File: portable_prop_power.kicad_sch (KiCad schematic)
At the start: 10 parts

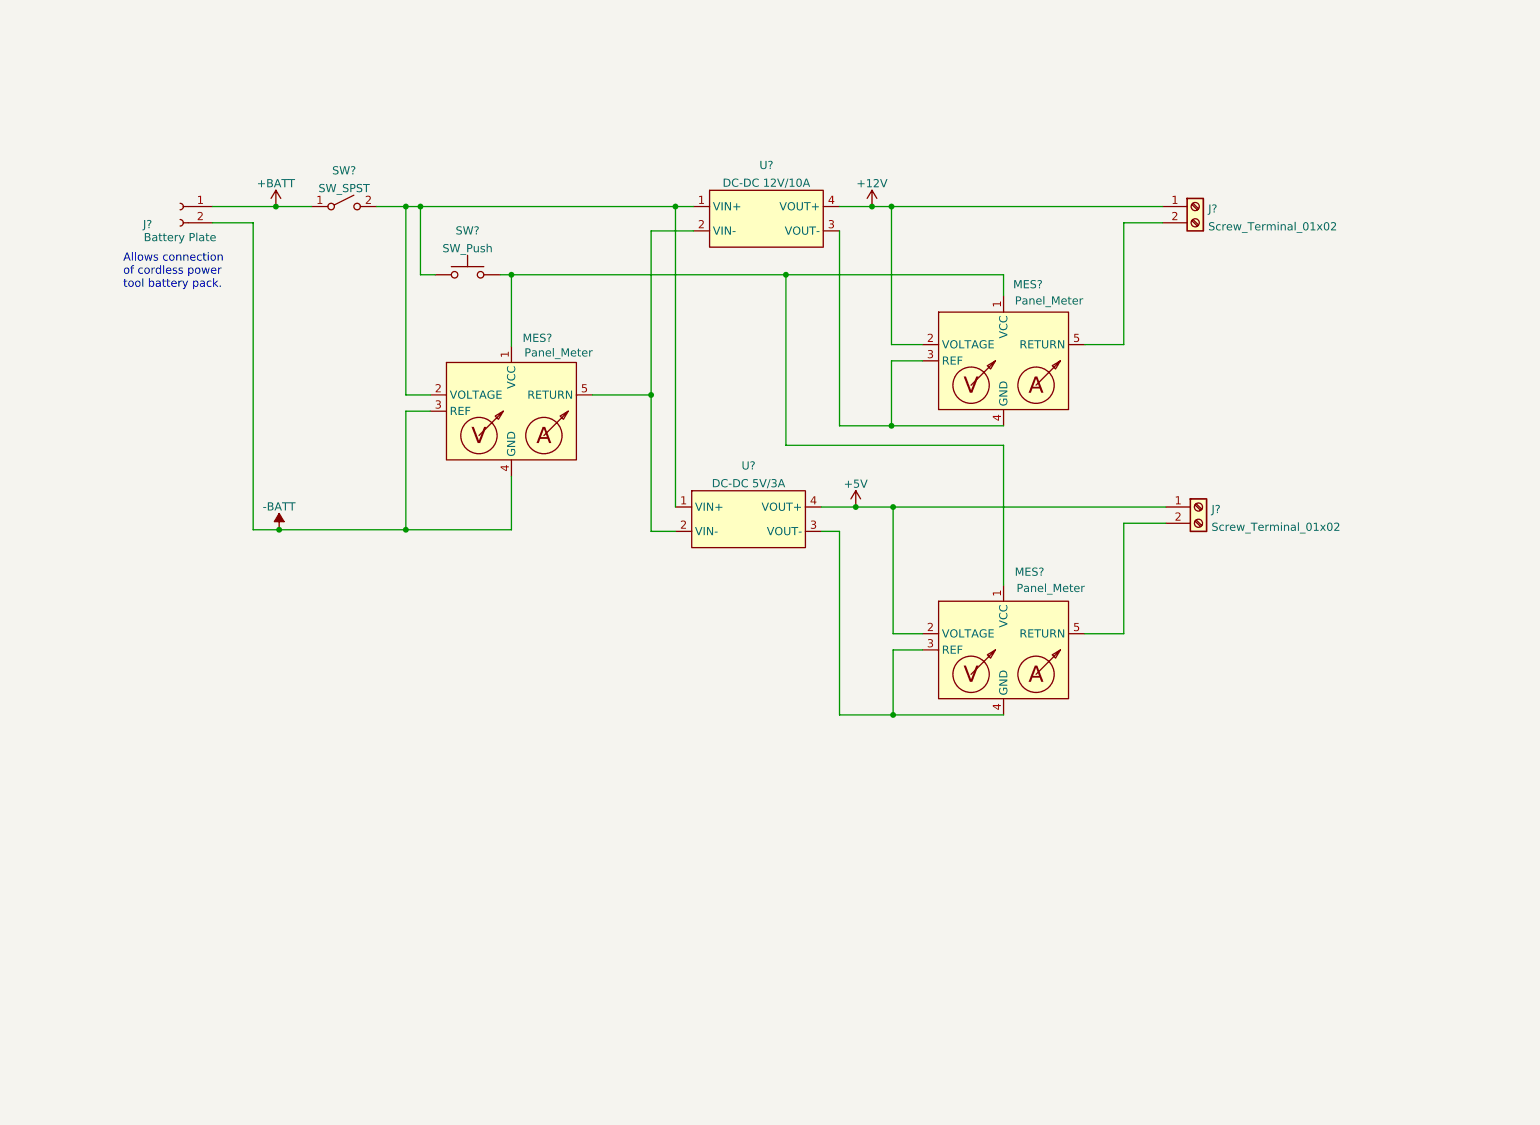
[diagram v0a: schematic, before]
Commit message: Iterated on the wiring diagram. Eliminated one connector.
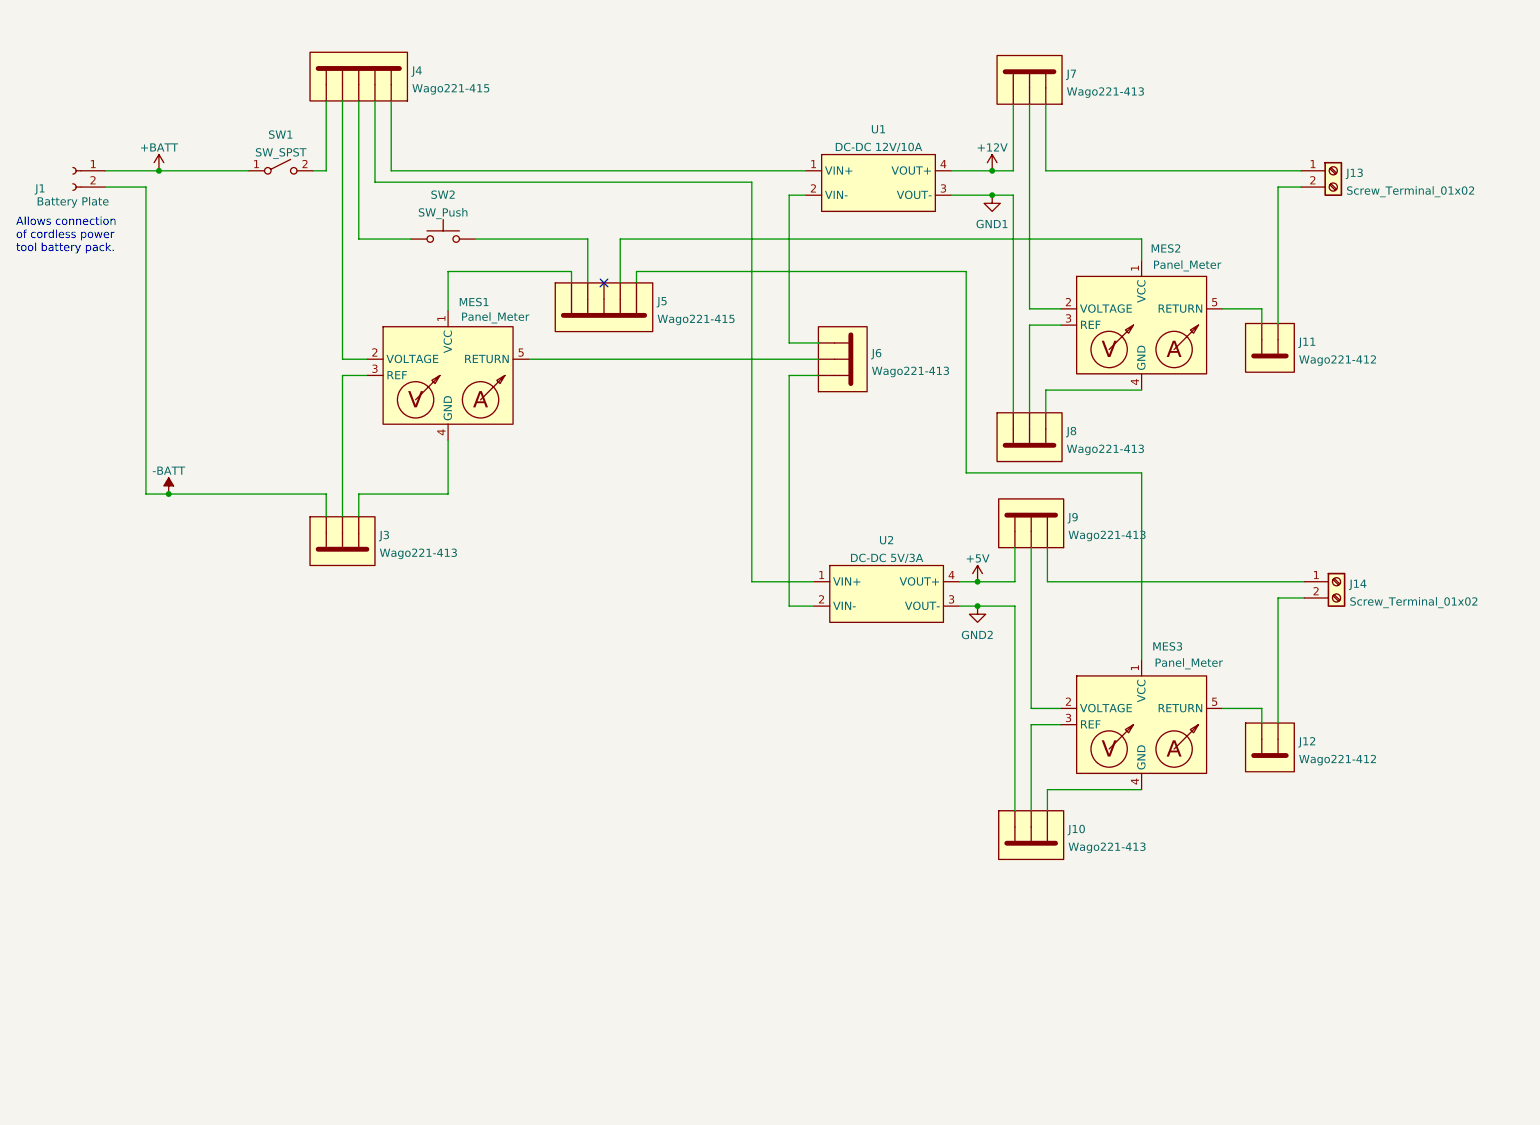
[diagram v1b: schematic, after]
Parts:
- added J10, J3, J6, J7, J8, J9: Wago221-413, symbol aid_Mechanical:Wago221-413
- added J11, J12: Wago221-412, symbol aid_Mechanical:Wago221-412
- added J4, J5: Wago221-415, symbol aid_Mechanical:Wago221-415
- gave numbers to parts that had none: 10
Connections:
- net +12V: now also J7.3; no longer J13.1 (Pin_1), MES2.2 (VOLTAGE)
- net +5V: now also J9.3; no longer J14.1 (Pin_1), MES3.2 (VOLTAGE)
- net -BATT: now also J3.1; no longer MES1.3 (REF), MES1.4 (GND)
- net at MES3.5 (RETURN): now also J12.1; no longer J14.2 (Pin_2)
- net at MES2.5 (RETURN): now also J11.1; no longer J13.2 (Pin_2)
- new net: J4.1, U1.1 (VIN+)
- new net: J6.3, U1.2 (VIN-)
- new net: J5.5, MES3.1 (VCC)
- new net: J9.2, MES3.2 (VOLTAGE)
- new net: J10.2, MES3.3 (REF)
- new net: J10.3, MES3.4 (GND)
- new net: J3.2, MES1.3 (REF)
- new net: J3.3, MES1.4 (GND)
- new net: J8.2, MES2.3 (REF)
- new net: J8.3, MES2.4 (GND)
- new net: J12.2, J14.2 (Pin_2)
- new net: J5.1, MES1.1 (VCC)
- new net: J5.2, SW2.2
- new net: J5.4, MES2.1 (VCC)
- new net: J11.2, J13.2 (Pin_2)
- new net: J4.2, U2.1 (VIN+)
- new net: J4.3, SW2.1
- new net: J4.4, MES1.2 (VOLTAGE)
- new net: J4.5, SW1.2 (B)
- new net: J7.2, MES2.2 (VOLTAGE)
- new net: J14.1 (Pin_1), J9.1
- new net: J6.1, U2.2 (VIN-)
- new net: J6.2, MES1.5 (RETURN)
- new net: J13.1 (Pin_1), J7.1
- new net GND1: J8.1, U1.3 (VOUT-)
- new net GND2: J10.1, U2.3 (VOUT-)
- no-connect marks 0 -> 1
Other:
- moved on the sheet: J1, J13, J14, MES1, MES2, MES3, SW1, SW2, U1, U2

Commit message: Reworked schematic again.
* Removed the dipictions of the lever nuts.
* Updated the symbols for the panel meters and added a note.
* Corrected panel meter connections after reviewing seller's diagrams.
* Adjusted layout to separate the panel-mount components from the ones
in the box in an effort to find better ways to make all of the wiring
connections.
* Added a fuse.
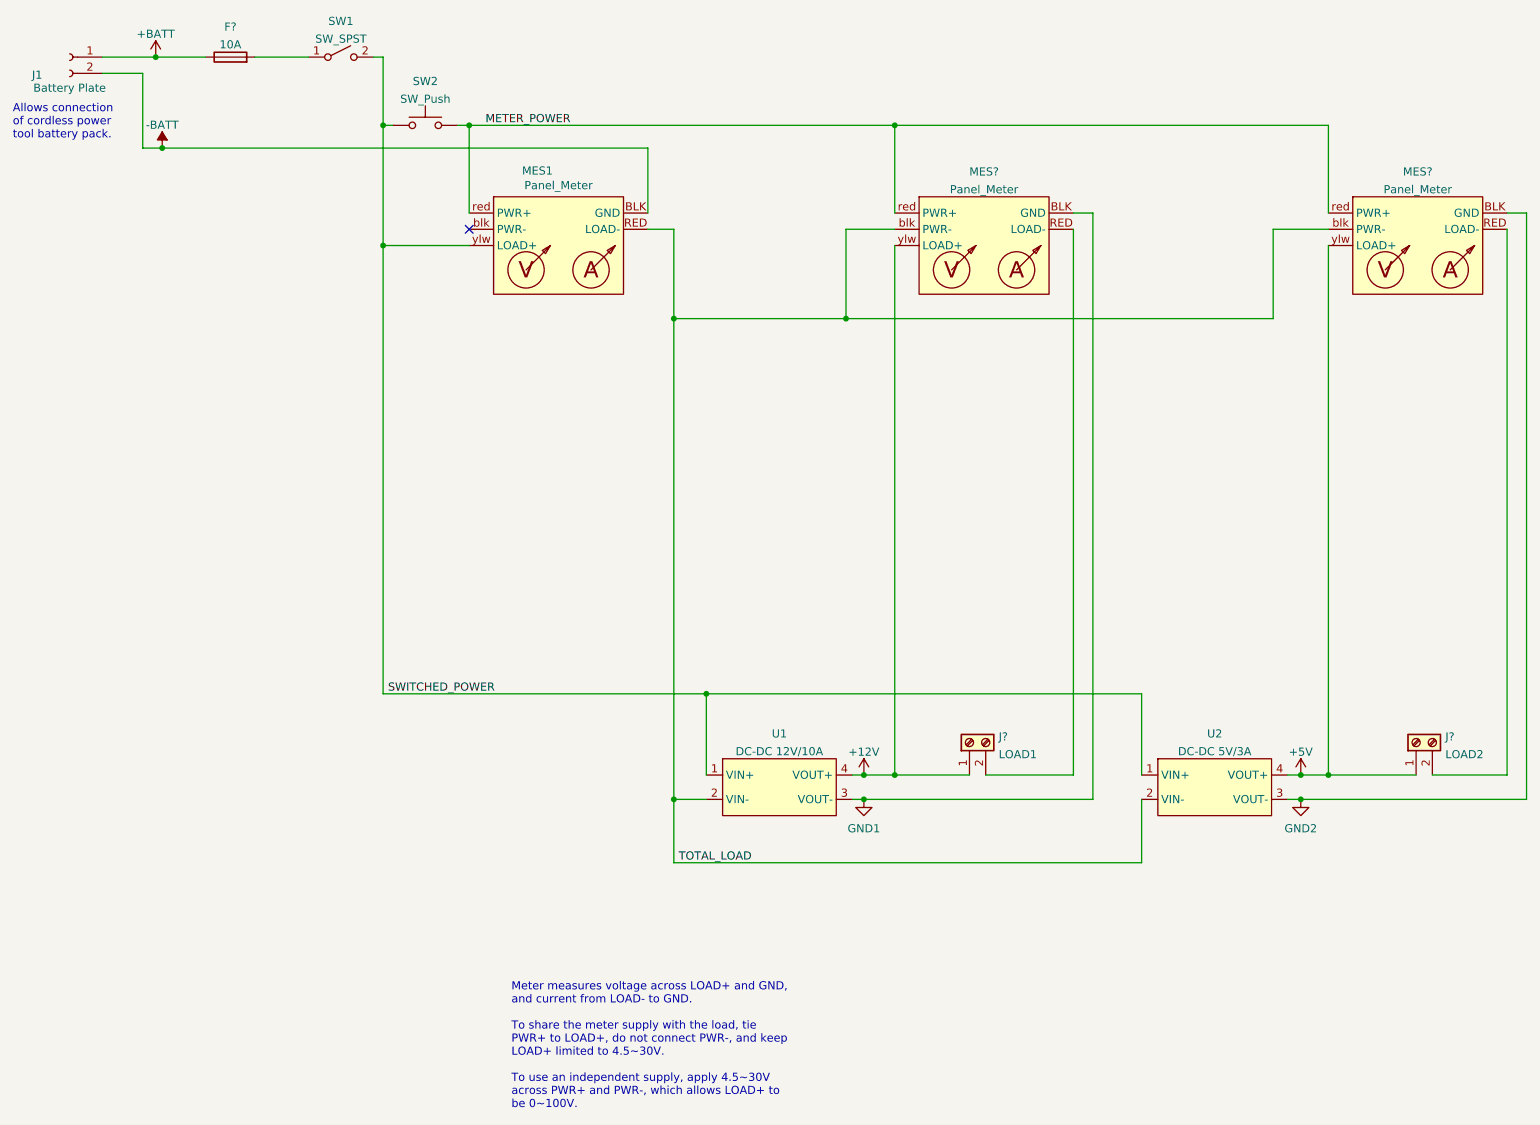
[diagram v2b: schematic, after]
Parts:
- removed J10, J3, J6, J7, J8, J9: Wago221-413, symbol aid_Mechanical:Wago221-413
- removed J11, J12: Wago221-412, symbol aid_Mechanical:Wago221-412
- removed J13, J14: Screw_Terminal_01x02, symbol Connector:Screw_Terminal_01x02
- removed J4, J5: Wago221-415, symbol aid_Mechanical:Wago221-415
- removed MES2, MES3: Panel_Meter, symbol aid_Modules:Panel_Meter
- added F?: 10A, symbol Device:Fuse
- added J?: LOAD1, symbol Connector:Screw_Terminal_01x02
- added J?: LOAD2, symbol Connector:Screw_Terminal_01x02
- added MES? (x2): Panel_Meter, symbol aid_Modules:Panel_Meter
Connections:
- net +12V: now also J?.1 (Pin_1), MES?.ylw (LOAD+)
- net +5V: now also J?.1 (Pin_1), MES?.ylw (LOAD+)
- net +BATT: now also F?.1; no longer SW1.1 (A)
- net -BATT: now also MES1.BLK (GND)
- net GND1: now also MES?.BLK (GND)
- net GND2: now also MES?.BLK (GND)
- net SWITCHED_POWER: now reaches U1.1 (VIN+)
- net SWITCHED_POWER: now also MES1.ylw (LOAD+), SW1.2 (B), SW2.1, U2.1 (VIN+)
- net TOTAL_LOAD: now reaches U1.2 (VIN-)
- net TOTAL_LOAD: now also MES1.RED (LOAD-), U2.2 (VIN-), MES?.blk (PWR-), MES?.blk (PWR-)
- net METER_POWER: now reaches SW2.2
- net METER_POWER: now also MES1.red (PWR+), MES?.red (PWR+), MES?.red (PWR+)
- new net: J?.2 (Pin_2), MES?.RED (LOAD-) (x2)
- new net: F?.2, SW1.1 (A)
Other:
- note added: "Meter measures voltage across LOAD+ and GND, and current from LOAD- to GND. To share the meter supply with the load, tie PWR+ to LOAD+, do not connect PWR-, and keep LOAD+ limited to 4.5~30V. To use an independent supply, apply 4.5~30V across PWR+ and PWR-, which allows LOAD+ to be 0~100V."
- moved on the sheet: J1, MES1, SW1, SW2, U1, U2

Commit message: Added wire color notations to schematic.
I'm not sure whether that's a good color scheme, but it's something I'm
considering to make it simpler to wire correctly.
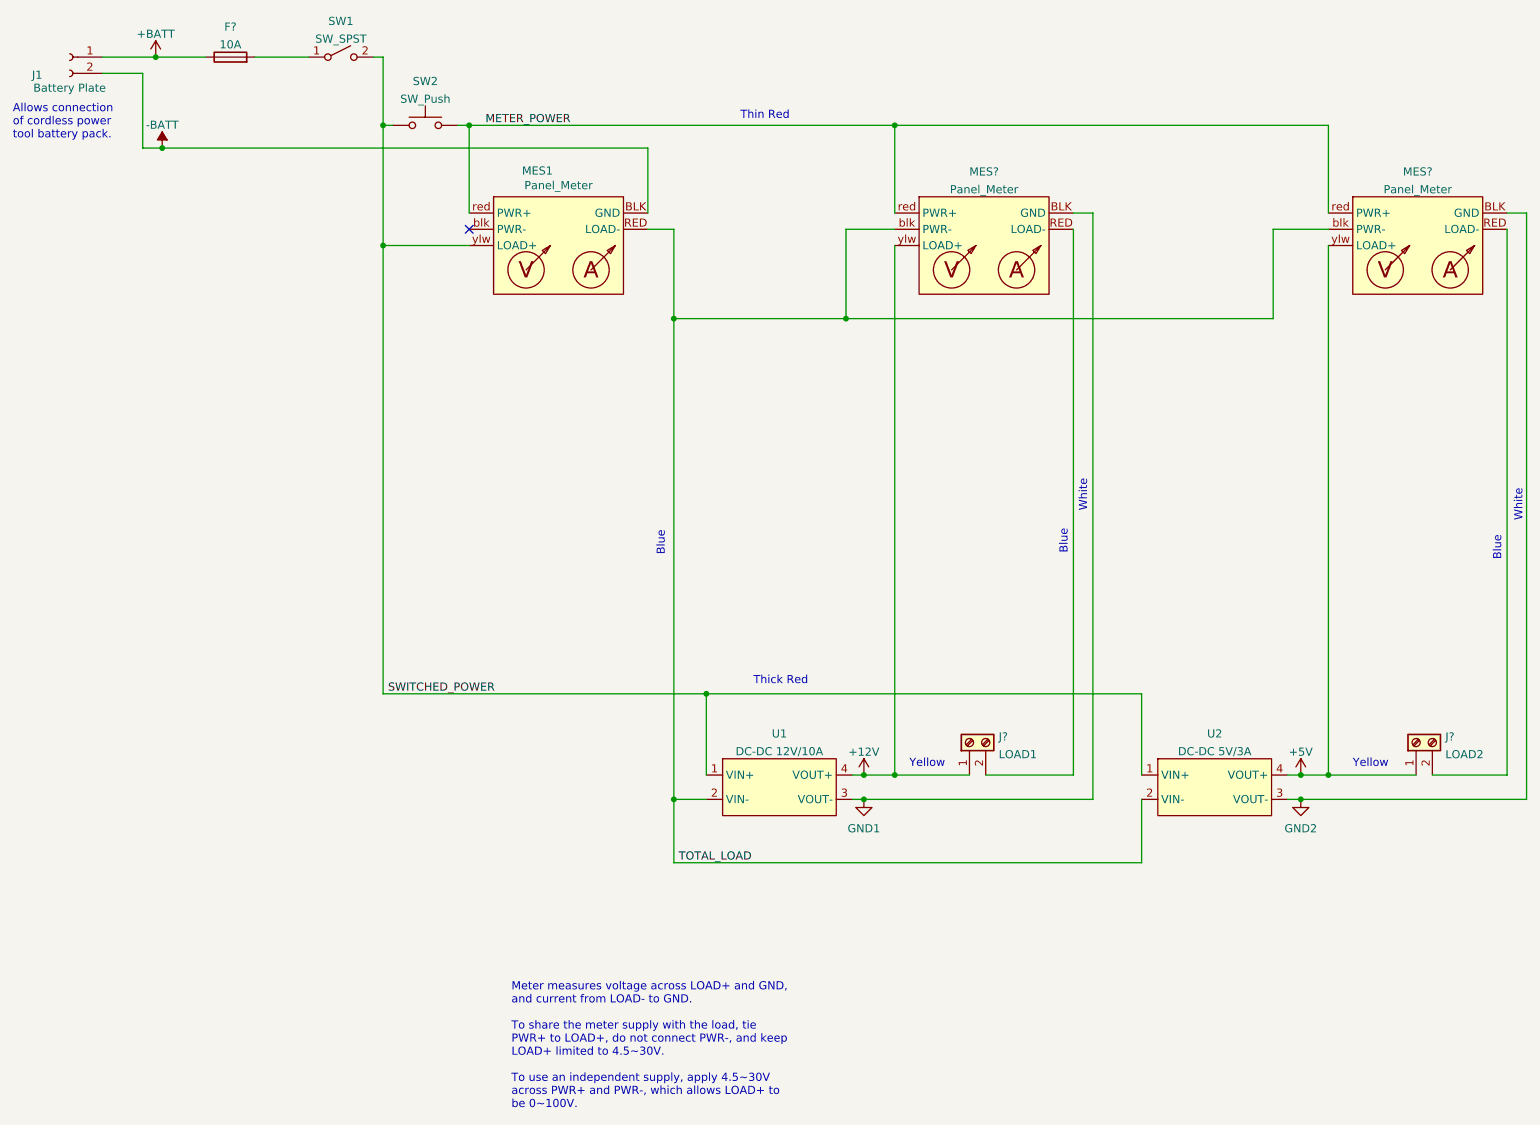
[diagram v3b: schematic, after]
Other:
- note added: "Blue"
- note added: "Thick Red"
- note added: "Thin Red"
- note added: "White"
- note added: "Yellow"
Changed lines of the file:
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@@
     (stroke (width 0) (type default) (color 0 0 0 0))
+  )
+  (text "Thin Red" (at 137.414 39.878 0)
+    (effects (font (size 1.27 1.27)) (justify left bottom))
+  )
+  (text "Yellow" (at 163.83 141.224 0)
+    (effects (font (size 1.27 1.27)) (justify left bottom))
+  )
+  (text "Blue" (at 256.54 108.712 90)
+    (effects (font (size 1.27 1.27)) (justify left bottom))
+  )
+  (text "Thick Red" (at 139.446 128.27 0)
+    (effects (font (size 1.27 1.27)) (justify left bottom))
   )
   (text "Allows connection\nof cordless power\ntool battery pack."
@@
     (effects (font (size 1.27 1.27)) (justify left bottom))
   )
+  (text "Yellow\n" (at 233.172 141.224 0)
+    (effects (font (size 1.27 1.27)) (justify left bottom))
+  )
+  (text "Blue" (at 125.73 107.95 90)
+    (effects (font (size 1.27 1.27)) (justify left bottom))
+  )
+  (text "Blue" (at 188.722 107.696 90)
+    (effects (font (size 1.27 1.27)) (justify left bottom))
+  )
+  (text "White" (at 259.842 102.616 90)
+    (effects (font (size 1.27 1.27)) (justify left bottom))
+  )
+  (text "White" (at 191.77 101.092 90)
+    (effects (font (size 1.27 1.27)) (justify left bottom))
+  )
